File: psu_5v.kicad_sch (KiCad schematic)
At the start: 8 parts, among them U2 LM2596S-ADJ

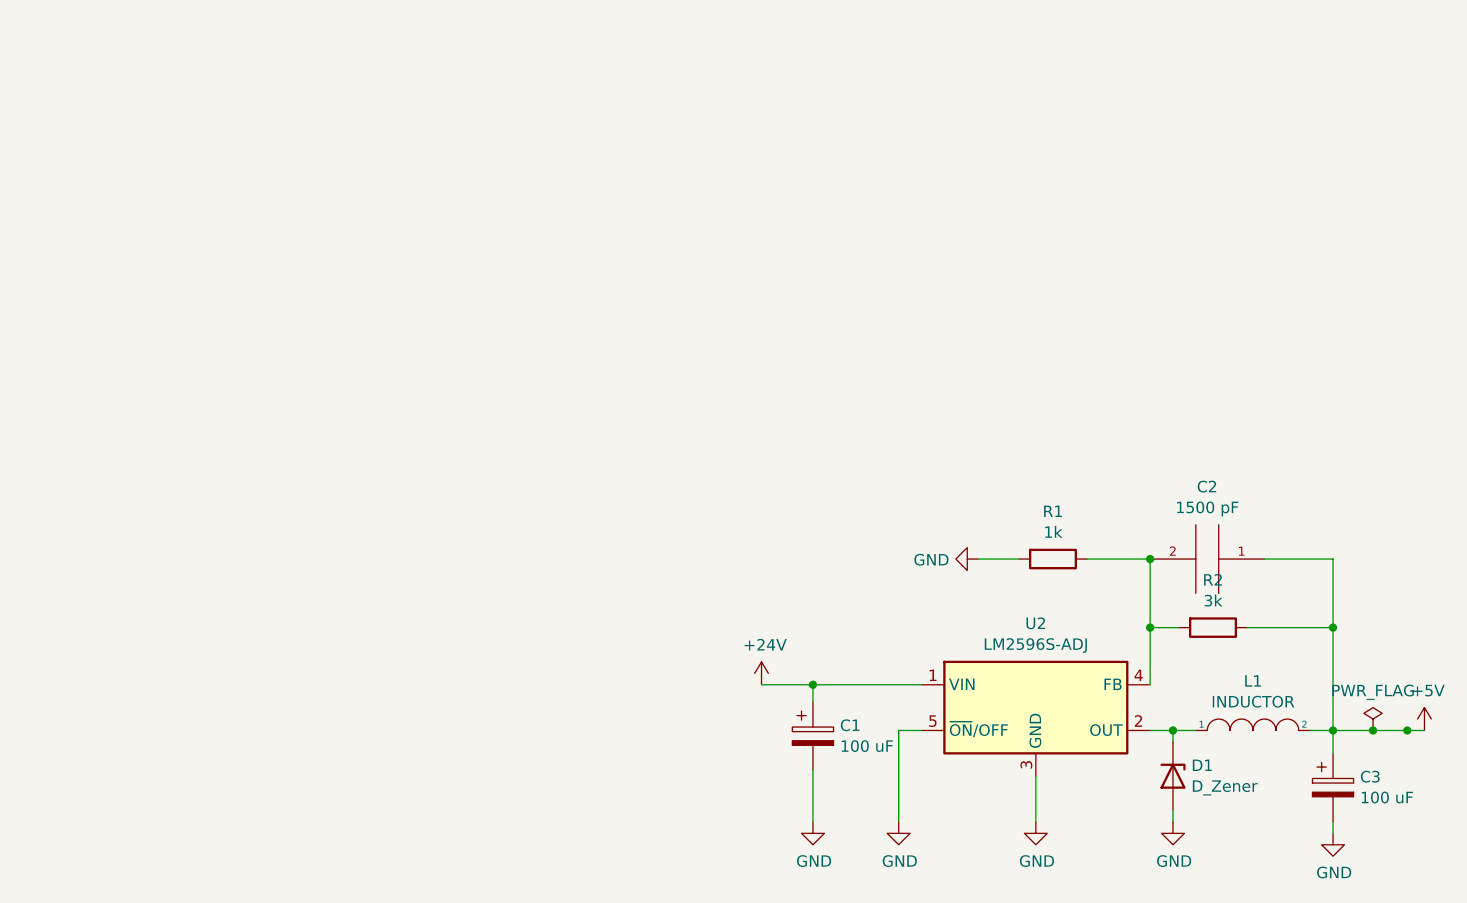
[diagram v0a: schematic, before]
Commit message: WIP: J18/Q2/Q3/R30/R31 + reguardado KiCad de todas las hojas
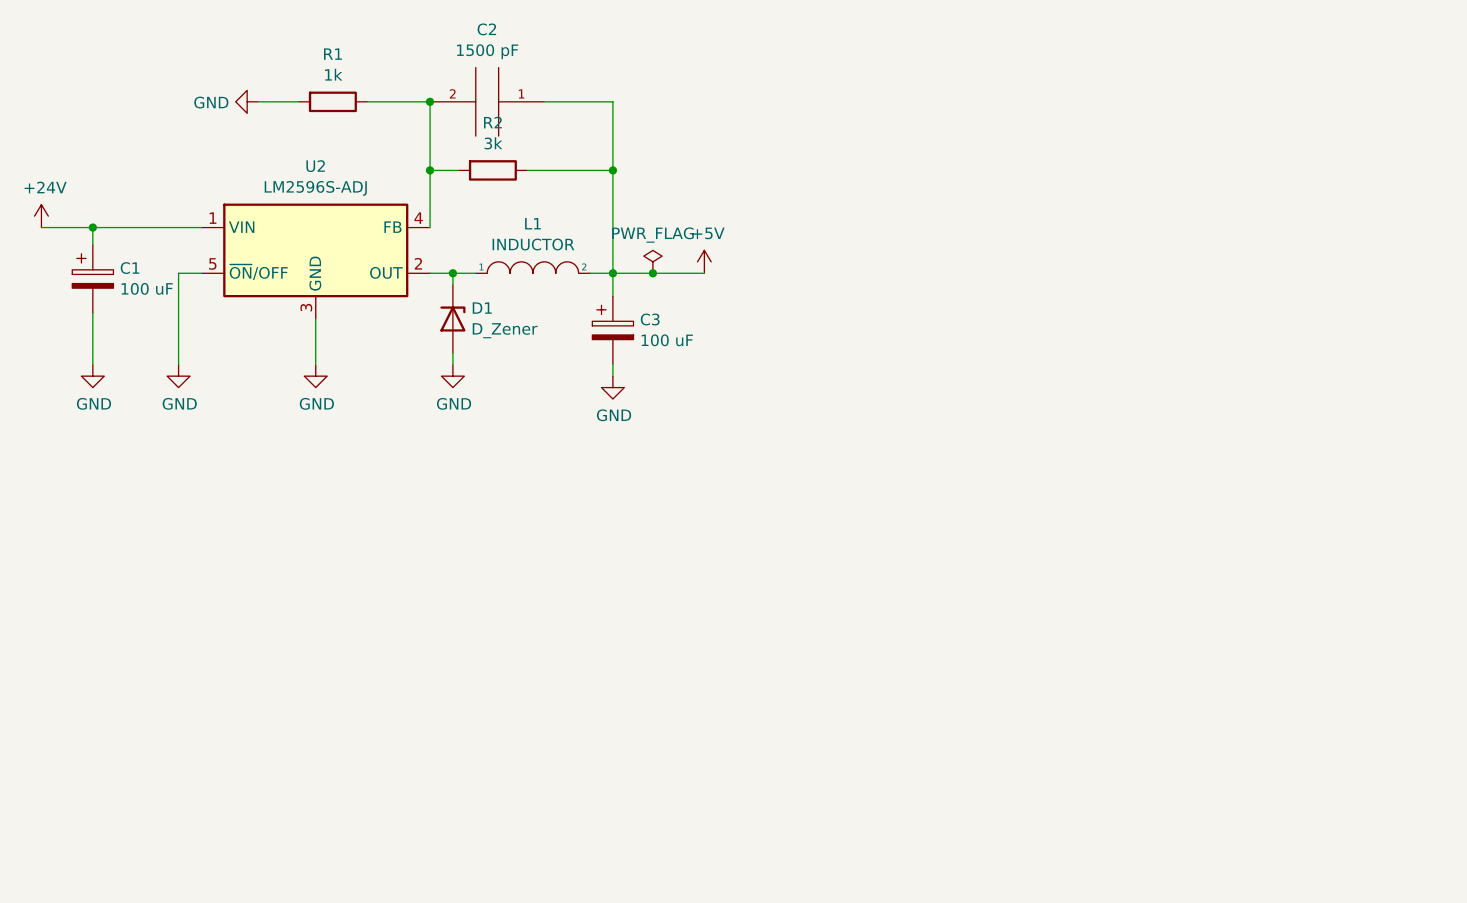
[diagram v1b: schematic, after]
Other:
- moved on the sheet: C1, C2, C3, D1, L1, R1, R2, U2

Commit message: friday changes
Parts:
- removed C1, C3: 100 uF, Capacitor_SMD:CP_Elec_8x10.5, symbol Device:CP
- removed C2: 1500 pF, Capacitor_SMD:C_0805_2012Metric_Pad1.18x1.45mm_HandSolder, symbol pspice:CAP
- removed D1: D_Zener, Diode_SMD:D_2114_3652Metric, symbol Device:D_Zener
- removed L1: INDUCTOR, Inductor_SMD:L_Bourns_SDR1806, symbol pspice:INDUCTOR
- removed R1: 1k, Resistor_SMD:R_1206_3216Metric_Pad1.30x1.75mm_HandSolder, symbol Device:R
- removed R2: 3k, Resistor_SMD:R_1206_3216Metric_Pad1.30x1.75mm_HandSolder, symbol Device:R
- removed U2: LM2596S-ADJ, Package_TO_SOT_SMD:TO-263-5_TabPin3, symbol Regulator_Switching:LM2596S-ADJ
- added C44, C45: 4.7uF, Capacitor_SMD:C_1210_3225Metric, symbol Device:C
- added C46: 47nF, Capacitor_SMD:C_0805_2012Metric, symbol Device:C
- added C47, C48, C49: 47uF, Capacitor_SMD:C_1210_3225Metric, symbol Device:C
- added C50: 120pF, Capacitor_SMD:C_0402_1005Metric, symbol Device:C
- added C51: 0.47uF, Capacitor_SMD:C_0603_1608Metric, symbol Device:C
- added C52: 2.2uF, Capacitor_SMD:C_0603_1608Metric, symbol Device:C
- added C53: 1uF, Capacitor_SMD:C_0603_1608Metric, symbol Device:C
- added C54: 22nF, Capacitor_SMD:C_0402_1005Metric, symbol Device:C
- added L4: 10uH, Inductor_SMD:L_Bourns_SRR1260, symbol Device:L
- added R101: 402k, Resistor_SMD:R_0402_1005Metric, symbol Device:R
- added R102, R105, R106: 100k, Resistor_SMD:R_0402_1005Metric, symbol Device:R
- added R103: 78.7k, Resistor_SMD:R_0402_1005Metric, symbol Device:R
- added R104: 1.21M, Resistor_SMD:R_0402_1005Metric, symbol Device:R
- added U2: LM76003, Package_DFN_QFN:Texas_RNP0030B_WQFN-30-1EP_4x6mm_P0.5mm_EP1.8x4.5mm_ThermalVias, symbol Regulator_Switching:LM76003
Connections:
- net +24V: now also C44.1, C45.1, C46.1, R104.1, U2.20 (PVIN), U2.21 (PVIN), U2.22 (PVIN)
- net +5V: now also C47.1, C48.1, C49.1, C50.1, C53.1, L4.2, R101.1, R106.1, U2.9 (BIAS)
- net GND: now also C44.2, C45.2, C46.2, C47.2, C48.2, C49.2, C52.2, C53.2, C54.2, R102.2, R103.2, R105.2, U2.13 (AGND), U2.14 (AGND), U2.15 (AGND), U2.17 (SYNC/MODE), U2.19 (NC_{GND}), U2.24 (PGND), U2.25 (PGND), U2.26 (PGND), U2.27 (NC_{GND}), U2.28 (NC_{GND}), U2.29 (NC_{GND}), U2.30 (NC_{GND}), U2.31 (AGND)
- new net PSU5_BOOT: C51.1, U2.6 (BOOT)
- new net PSU5_EN: R104.2, R105.1, U2.18 (EN)
- new net PSU5_FB: C50.2, R101.2, R102.1, U2.12 (FB)
- new net PSU5_PG: R106.2, U2.16 (PGOOD)
- new net PSU5_RT: R103.1, U2.10 (RT)
- new net PSU5_SS: C54.1, U2.11 (SS/TRK)
- new net PSU5_SW: C51.2, L4.1, U2.1 (SW), U2.2 (SW), U2.3 (SW), U2.4 (SW), U2.5 (SW)
- new net PSU5_VCC: C52.1, U2.8 (VCC)
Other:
- title: PSU 5V - Convertidor reductor LM2596S-ADJ (+24V -> +5V) -> PSU 5V - Convertidor reductor sincrono LM76003 (+24V -> +5V)

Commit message: schematic updated
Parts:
- renumbered C53 to C10, C44 to C11, C45 to C12, C46 to C13, C47 to C14, C48 to C15, C49 to C16, C50 to C17, C54 to C18, C51 to C8, C52 to C9, L4 to L1, R101 to R12, R102 to R13, R103 to R14, R104 to R15, R105 to R16, R106 to R17, U2 to U3
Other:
- moved on the sheet: C17, C18, L1, R12, R13, R14, R15, R16, R17

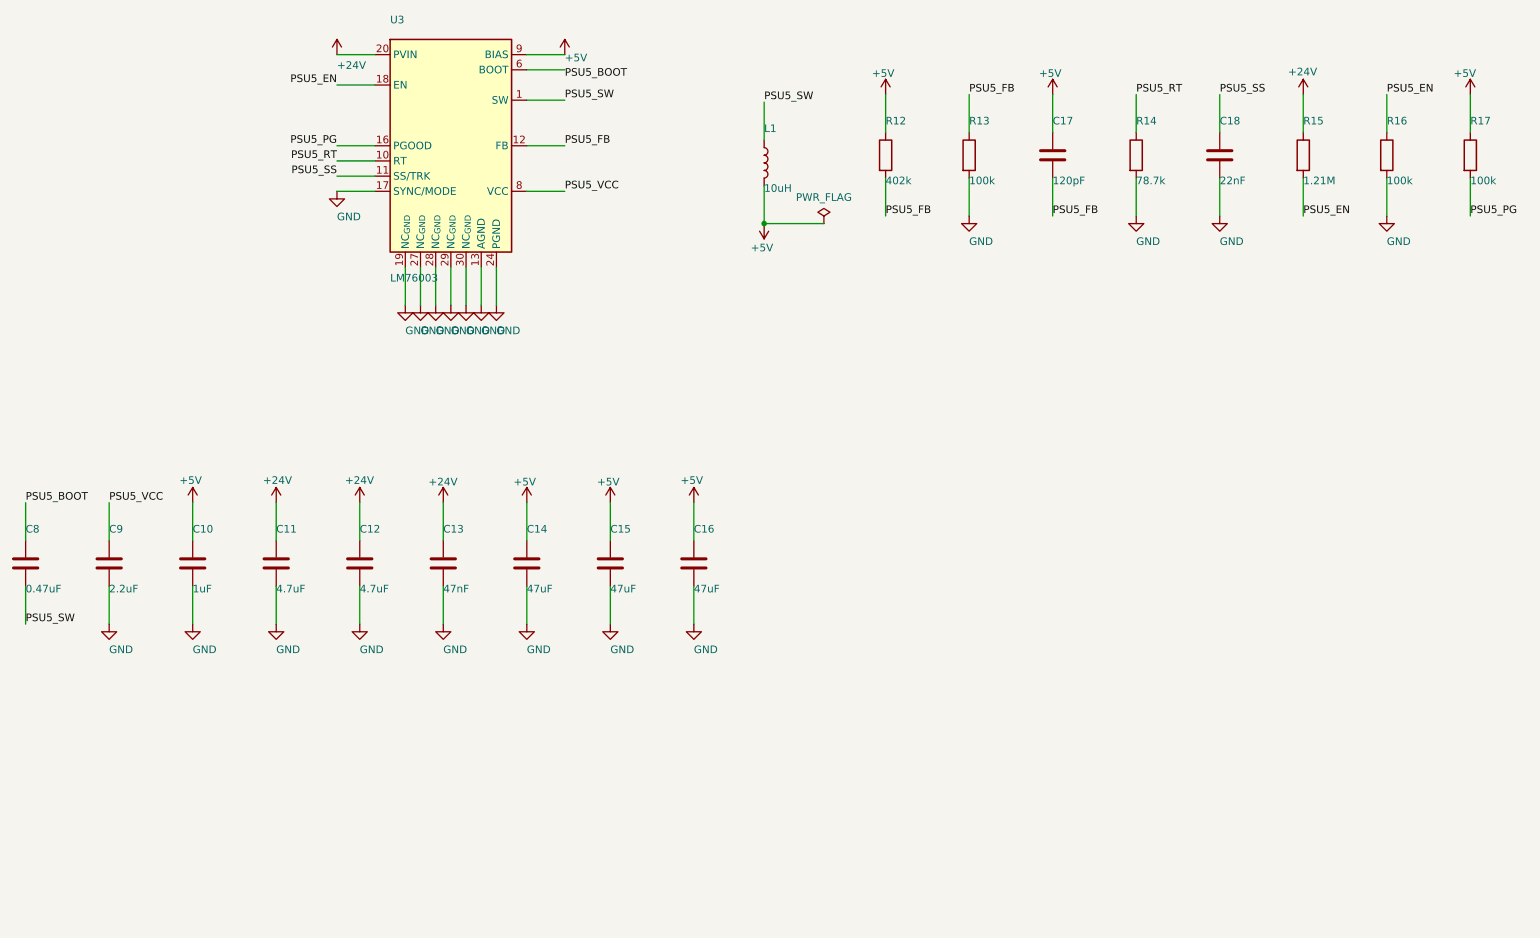
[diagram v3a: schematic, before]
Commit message: 2 power source
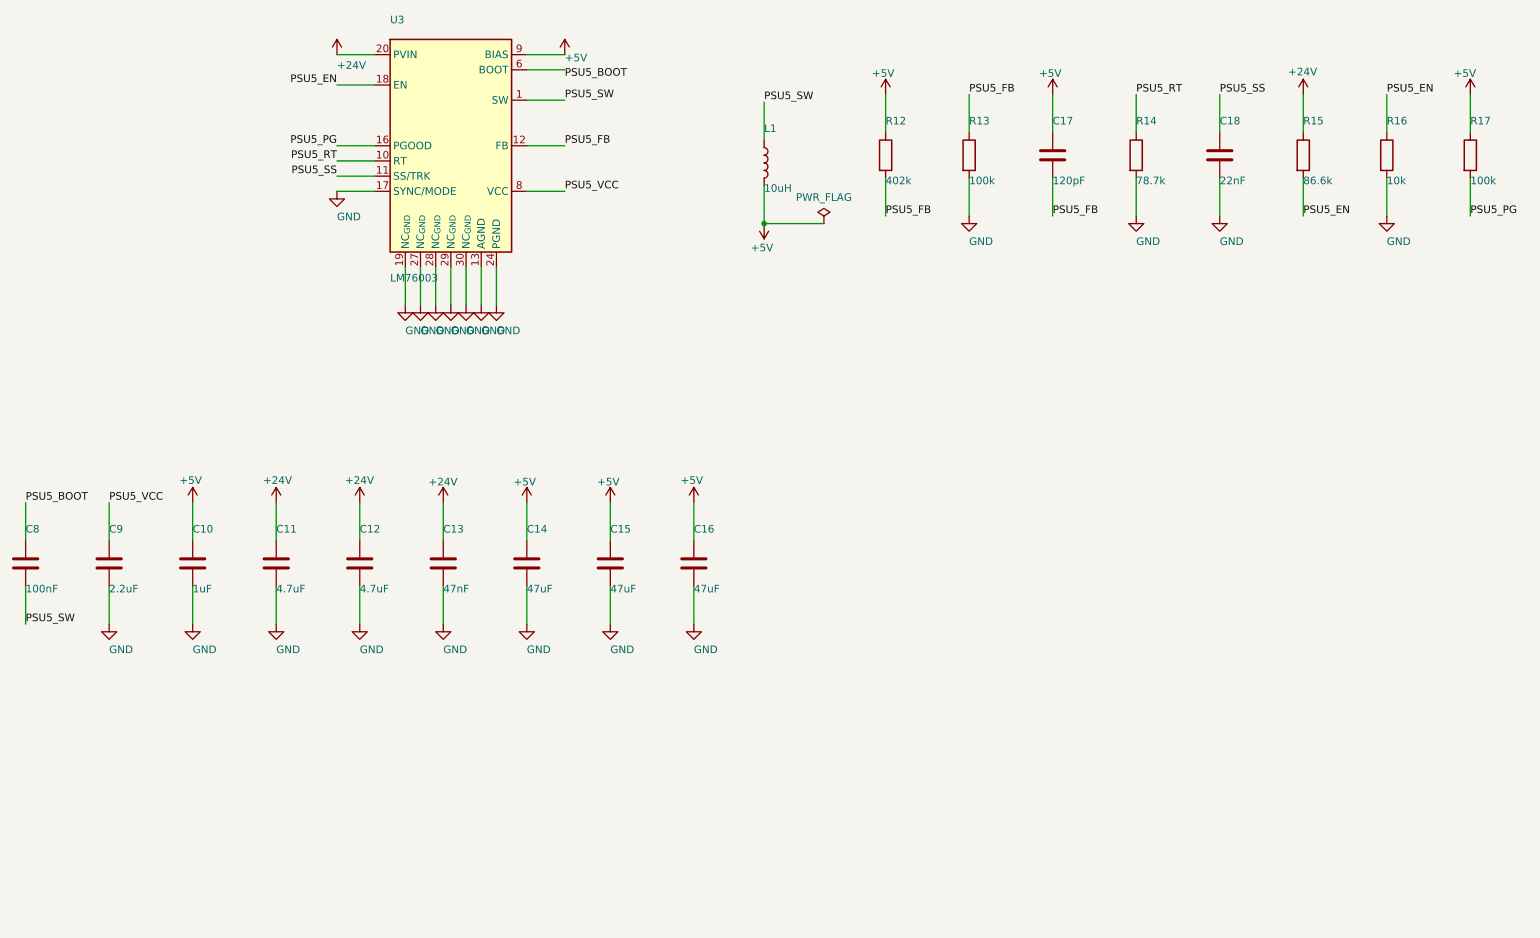
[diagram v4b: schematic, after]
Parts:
- C8: value 0.47uF -> 100nF; DigiKey 1276-2082-2-ND -> 1276-1000-1-ND; MPN CL10B474KA8NFNC -> CL10B104KB8NNNC
- R15: value 1.21M -> 86.6k; DigiKey RMCF0402FT1M21TR-ND -> RMCF0402FT86K6TR-ND; MPN RMCF0402FT1M21 -> RMCF0402FT86K6
- R16: value 100k -> 10k; DigiKey 311-100KLRTR-ND -> 311-10.0KLRTR-ND; MPN RC0402FR-07100KL -> RC0402FR-0710KL
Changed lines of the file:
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@@
 			)
 		)
-		(property "Value" "1.21M"
+		(property "Value" "86.6k"
 			(at 233.68 46.91 0)
 			(effects
@@
 			)
 		)
-		(property "MPN" "RMCF0402FT1M21"
+		(property "MPN" "RMCF0402FT86K6"
 			(at 129.86 -44.13 0)
 			(effects
@@
 			)
 		)
-		(property "DigiKey" "RMCF0402FT1M21TR-ND"
+		(property "DigiKey" "RMCF0402FT86K6TR-ND"
 			(at 129.86 -44.13 0)
 			(effects
@@
 			)
 		)
-		(property "Value" "0.47uF"
+		(property "Value" "100nF"
 			(at 20 115.17 0)
 			(effects
@@
 			)
 		)
-		(property "MPN" "CL10B474KA8NFNC"
+		(property "MPN" "CL10B104KB8NNNC"
 			(at 0 0 0)
 			(effects
@@
 			)
 		)
-		(property "DigiKey" "1276-2082-2-ND"
+		(property "DigiKey" "1276-1000-1-ND"
 			(at 0 0 0)
 			(effects
@@
 			)
 		)
-		(property "Value" "100k"
+		(property "Value" "10k"
 			(at 247.65 46.91 0)
 			(effects
@@
 			)
 		)
-		(property "MPN" "RC0402FR-07100KL"
+		(property "MPN" "RC0402FR-0710KL"
 			(at 129.86 -44.13 0)
 			(effects
@@
 			)
 		)
-		(property "DigiKey" "311-100KLRTR-ND"
+		(property "DigiKey" "311-10.0KLRTR-ND"
 			(at 129.86 -44.13 0)
 			(effects

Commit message: last changes in work
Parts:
- C14, C15, C16: value 47uF -> 33uF; DigiKey 490-16309-2-ND -> (none); MPN GRM32EC81C476KE15K -> (none); Manufacturer Murata Electronics -> (none)
- C17: value 120pF -> 47pF; DigiKey 490-1292-2-ND -> 490-5942-1-ND; MPN GRM1555C1H121JA01D -> GRM1555C1H470JA01D
- C8: value 100nF -> 470nF; DigiKey 1276-1000-1-ND -> 490-3291-1-ND; MPN CL10B104KB8NNNC -> GRM188R71E474KA12D; Manufacturer Samsung Electro-Mechanics -> Murata Electronics
- L1: value 10uH -> 6.8uH; DigiKey SRP1265A-100MTR-ND -> SRP1265A-6R8MCT-ND; MPN SRP1265A-100M -> SRP1265A-6R8M
- R12: value 402k -> 100k; DigiKey YAG3151TR-ND -> 311-100KLRTR-ND; MPN RC0402FR-07402KL -> RC0402FR-07100KL
- R13: value 100k -> 24.9k; DigiKey 311-100KLRTR-ND -> 311-24.9KLRCT-ND; MPN RC0402FR-07100KL -> RC0402FR-0724K9L
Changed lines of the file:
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@@
 			)
 		)
-		(property "Value" "100k"
+		(property "Value" "24.9k"
 			(at 177.8 46.91 0)
 			(effects
@@
 			)
 		)
-		(property "MPN" "RC0402FR-07100KL"
+		(property "MPN" "RC0402FR-0724K9L"
 			(at 129.86 -44.13 0)
 			(effects
@@
 			)
 		)
-		(property "DigiKey" "311-100KLRTR-ND"
+		(property "DigiKey" "311-24.9KLRCT-ND"
 			(at 129.86 -44.13 0)
 			(effects
@@
 			)
 		)
-		(property "Value" "10uH"
+		(property "Value" "6.8uH"
 			(at 143.51 48.18 0)
 			(effects
@@
 			)
 		)
-		(property "Description" "Power inductor, Isat 13A"
+		(property "Description" "Power inductor 6.8uH, Isat 18A / Irms 11.5A"
 			(at 143.51 43.18 0)
 			(effects
@@
 			)
 		)
-		(property "MPN" "SRP1265A-100M"
+		(property "MPN" "SRP1265A-6R8M"
 			(at 143.51 43.18 0)
 			(effects
@@
 			)
 		)
-		(property "DigiKey" "SRP1265A-100MTR-ND"
+		(property "DigiKey" "SRP1265A-6R8MCT-ND"
 			(at 123.51 -42.86 0)
 			(effects
@@
 			)
 		)
-		(property "Value" "47uF"
+		(property "Value" "33uF"
 			(at 131.76 115.17 0)
 			(effects
@@
 			)
 		)
-		(property "Description" "Salida ceramica 25V"
+		(property "Description" "Salida ceramica 33uF >=16V 1210 - MPN por definir"
 			(at 131.76 110.17 0)
 			(effects
@@
 			)
 		)
-		(property "Manufacturer" "Murata Electronics"
+		(property "Manufacturer" ""
 			(at 0 0 0)
 			(effects
@@
 			)
 		)
-		(property "MPN" "GRM32EC81C476KE15K"
+		(property "MPN" ""
 			(at 0 0 0)
 			(effects
@@
 			)
 		)
-		(property "DigiKey" "490-16309-2-ND"
+		(property "DigiKey" ""
 			(at 0 0 0)
 			(effects
@@
 			)
 		)
-		(property "Value" "402k"
+		(property "Value" "100k"
 			(at 163.83 46.91 0)
 			(effects
@@
 			)
 		)
-		(property "MPN" "RC0402FR-07402KL"
+		(property "MPN" "RC0402FR-07100KL"
 			(at 129.86 -44.13 0)
 			(effects
@@
 			)
 		)
-		(property "DigiKey" "YAG3151TR-ND"
+		(property "DigiKey" "311-100KLRTR-ND"
 			(at 129.86 -44.13 0)
 			(effects
@@
 			)
 		)
-		(property "Value" "47uF"
+		(property "Value" "33uF"
 			(at 103.82 115.17 0)
 			(effects
@@
 			)
 		)
-		(property "Description" "Salida ceramica 25V"
+		(property "Description" "Salida ceramica 33uF >=16V 1210 - MPN por definir"
 			(at 103.82 110.17 0)
 			(effects
@@
 			)
 		)
-		(property "Manufacturer" "Murata Electronics"
+		(property "Manufacturer" ""
 			(at 0 0 0)
 			(effects
@@
 			)
 		)
-		(property "MPN" "GRM32EC81C476KE15K"
+		(property "MPN" ""
 			(at 0 0 0)
 			(effects
@@
 			)
 		)
-		(property "DigiKey" "490-16309-2-ND"
+		(property "DigiKey" ""
 			(at 0 0 0)
 			(effects
@@
 		)
 		(property "Value" "+5V"
-			(at 110.17 26.35 0)
+			(at 107.696 22.098 0)
 			(effects
 				(font
@@
 			)
 		)
-		(property "Value" "100nF"
+		(property "Value" "470nF"
 			(at 20 115.17 0)
 			(effects
@@
 			)
 		)
-		(property "Manufacturer" "Samsung Electro-Mechanics"
+		(property "Manufacturer" "Murata Electronics"
 			(at 0 0 0)
 			(effects
@@
 			)
 		)
-		(property "MPN" "CL10B104KB8NNNC"
+		(property "MPN" "GRM188R71E474KA12D"
 			(at 0 0 0)
 			(effects
@@
 			)
 		)
-		(property "DigiKey" "1276-1000-1-ND"
+		(property "DigiKey" "490-3291-1-ND"
 			(at 0 0 0)
 			(effects
@@
 			)
 		)
-		(property "Value" "120pF"
+		(property "Value" "47pF"
 			(at 191.77 46.91 0)
 			(effects
@@
 			)
 		)
-		(property "Description" "Feed-forward, || R33"
+		(property "Description" "Feed-forward, || R12 (RFBT)"
 			(at 191.77 41.91 0)
 			(effects
@@
 			)
 		)
-		(property "MPN" "GRM1555C1H121JA01D"
+		(property "MPN" "GRM1555C1H470JA01D"
 			(at 129.86 -44.13 0)
 			(effects
@@
 			)
 		)
-		(property "DigiKey" "490-1292-2-ND"
+		(property "DigiKey" "490-5942-1-ND"
 			(at 129.86 -44.13 0)
 			(effects
@@
 			)
 		)
-		(property "Value" "47uF"
+		(property "Value" "33uF"
 			(at 117.79 115.17 0)
 			(effects
@@
 			)
 		)
-		(property "Description" "Salida ceramica 25V"
+		(property "Description" "Salida ceramica 33uF >=16V 1210 - MPN por definir"
 			(at 117.79 110.17 0)
 			(effects
@@
 			)
 		)
-		(property "Manufacturer" "Murata Electronics"
+		(property "Manufacturer" ""
 			(at 0 0 0)
 			(effects
@@
 			)
 		)
-		(property "MPN" "GRM32EC81C476KE15K"
+		(property "MPN" ""
 			(at 0 0 0)
 			(effects
@@
 			)
 		)
-		(property "DigiKey" "490-16309-2-ND"
+		(property "DigiKey" ""
 			(at 0 0 0)
 			(effects
